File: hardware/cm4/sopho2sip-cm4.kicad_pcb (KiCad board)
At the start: 4 copper layers, 110 x 85 mm, 88 parts, among them J10 USB-C 5V/USB, J11 CM4 Stecker 1, J12 CM4 Stecker 2, J13 microSD, J14 7499010211A, J15 Lüfter 5 V, J2 D340 Audio, J3 D340 PC-Schnittstelle, Q10 BSS84, Q11 AO3400A, SW1 Taste, SW2 Konfig, SW3 Ein/Aus, T1 SM-LP-5001, T2 SM-LP-5001, U10 USBLC6-2SC6, U11 AP22804AW5, U12 TPD4E05U06DQAR, U2 TLV320AIC3204IRHBR, U3 ADuM5211, U4 AP2112K-3.3, U5 MAX3232E, U6 12MHz

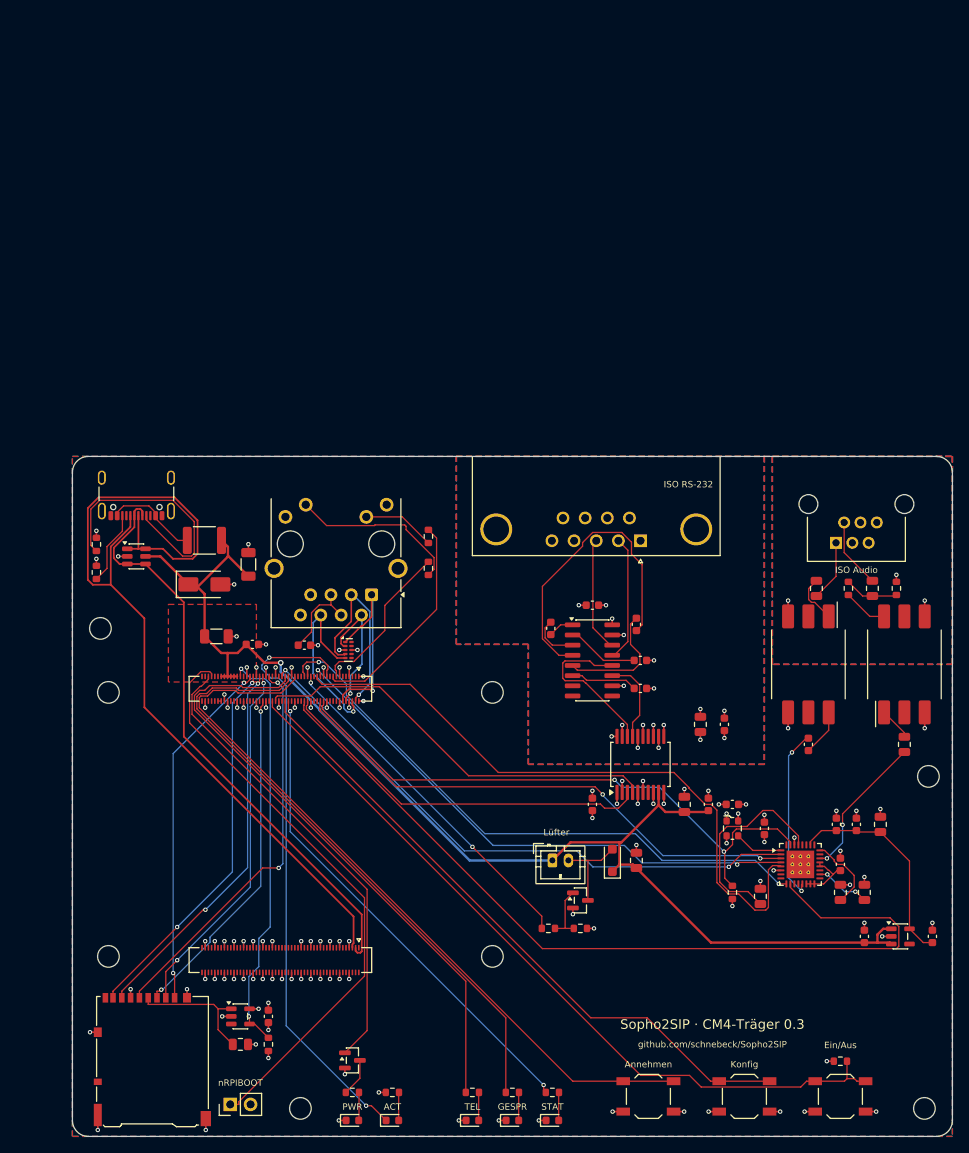
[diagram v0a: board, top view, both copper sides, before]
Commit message: CM4-Platine: Lage auf dem Blatt frei vom Schriftfeld, alle Bauteiltexte waagerecht
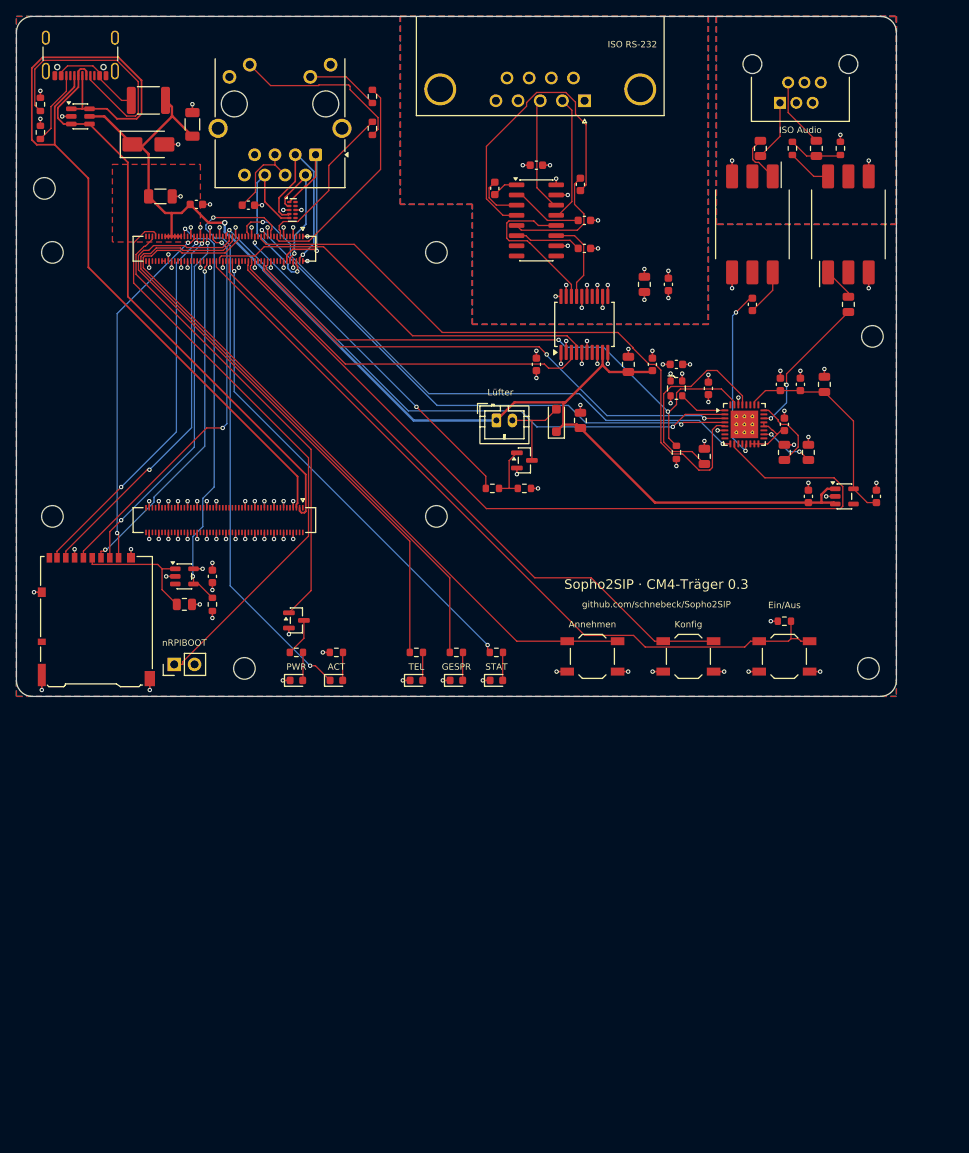
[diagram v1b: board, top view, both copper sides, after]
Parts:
- moved J12 55.4 mm to (119.0, 108.0)
- moved J10 55.4 mm to (101.0, 48.7)
- moved J14 55.4 mm to (130.4, 62.3)
- moved J3 55.4 mm to (164.0, 55.5)
- moved C12 55.4 mm to (179.5, 91.5)
- moved C14 55.4 mm to (188.5, 91.0)
- moved C15 55.4 mm to (191.0, 91.0)
- moved C16 55.4 mm to (194.0, 91.0)
- moved C17 55.4 mm to (189.0, 99.5)
- moved C18 55.4 mm to (179.0, 100.0)
- moved C19 55.4 mm to (192.0, 105.0)
- moved C20 55.4 mm to (200.5, 105.0)
- moved C21 55.4 mm to (186.0, 61.5)
- moved C22 55.4 mm to (185.0, 81.0)
- moved C23 55.4 mm to (197.0, 81.0)
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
